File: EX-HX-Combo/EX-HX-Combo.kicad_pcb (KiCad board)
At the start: 2 copper layers, 150.2 x 124.5 mm, 45 parts, among them CN1 DB9 Male, J1 IDE_CONNECTOR, J200 Bus_Tandy_Plus_Through, J3 Bus_Tandy_Plus, SW1 SW_DIP_x10, U1 BIOS FLASH, U2 74HCT245, U3 1.8432 MHz, U4 DS1315, U5 AS6C4008-55PCN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

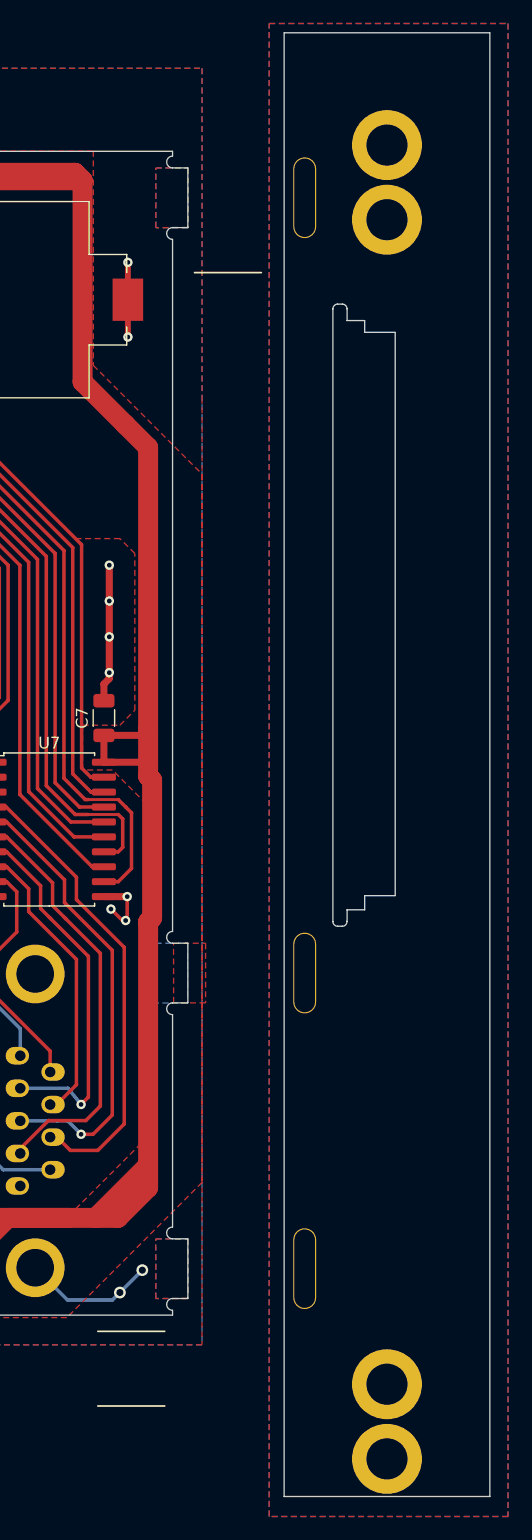
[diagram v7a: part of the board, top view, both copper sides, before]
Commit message: EX-HX-Combo layout work, including hole for DB-9 connector.
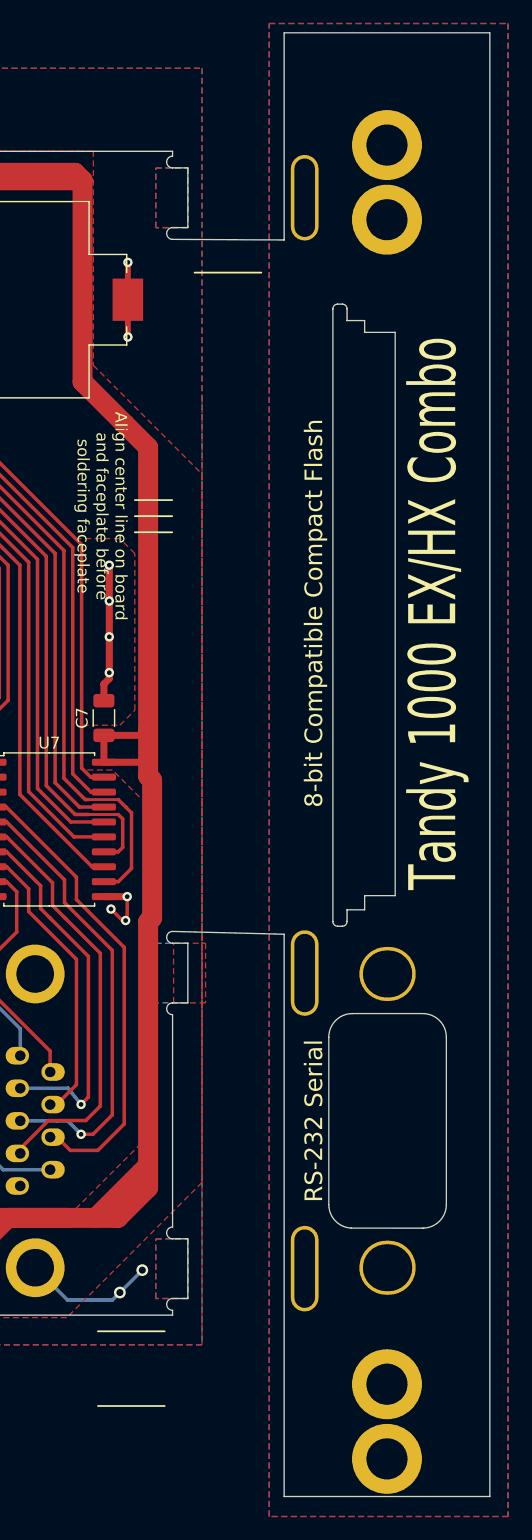
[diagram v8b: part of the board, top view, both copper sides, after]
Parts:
- added H8: DB-9 Faceplate, 00Custom:DB9_Face, F.Cu at (255.3, 120.0)
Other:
- outline, holes or cut-outs redrawn
- board text added: "8-bit Compatible Compact Flash"
- board text added: "Align center line on board and faceplate before soldering faceplate"
- board text added: "RS-232 Serial"
- board text added: "Tandy 1000 EX/HX Combo"
